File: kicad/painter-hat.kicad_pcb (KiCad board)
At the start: 2 copper layers, 64.6 x 55.8 mm, 45 parts, among them J1 Conn_01x08_Socket, J10 10137064-00021LF, J2 Conn_01x08_Socket, J3 Conn_01x08_Socket, J4 Conn_01x08_Socket, J5 Conn_02x20_Odd_Even, J6 Conn_01x04, J8 Conn_01x06_Pin, J9 Conn_01x04, Q1 NPN, Q2 NPN, Q4 Si2319CDS, Q5 Si2319CDS, U1 MAX26405AFOAY+T, U2 CYPD3177-24LQ, Y2 16 MHz

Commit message: feat: v2
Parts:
- removed J8: Conn_01x06_Pin, Connector_PinHeader_2.54mm:PinHeader_1x06_P2.54mm_Vertical
- removed Q1, Q2: NPN, Package_TO_SOT_THT:TO-92L_Inline_Wide
- removed Q5: Si2319CDS, Package_TO_SOT_SMD:SOT-23
- removed R1, R2, R3, R4: R, Resistor_SMD:R_0603_1608Metric
- added C12: 10uF, Capacitor_SMD:C_0603_1608Metric, F.Cu at (84.5, 94.1)
- added C13: 4.7uF, Capacitor_SMD:C_0603_1608Metric, F.Cu at (82.0, 92.6)
- added C14: 22uF, Capacitor_SMD:C_0805_2012Metric, F.Cu at (86.5, 86.1)
- added C15: 22uF, Capacitor_SMD:C_0805_2012Metric, F.Cu at (84.0, 86.1)
- added C16: 22uF, Capacitor_SMD:C_0805_2012Metric, F.Cu at (81.5, 86.1)
- added C17: 4.7uF, Capacitor_SMD:C_0603_1608Metric, F.Cu at (89.5, 93.8)
- added C18: 2.2uF, Capacitor_SMD:C_0603_1608Metric, F.Cu at (89.5, 91.3)
- added C19: 10nF, Capacitor_SMD:C_0402_1005Metric, F.Cu at (99.7, 98.0)
- added C20: 10nF, Capacitor_SMD:C_0402_1005Metric, F.Cu at (110.8, 89.6)
- added C21: 10nF, Capacitor_SMD:C_0402_1005Metric, F.Cu at (110.8, 90.8)
- added C22: 1uF, Capacitor_SMD:C_0805_2012Metric, F.Cu at (100.6, 130.0)
- added C23: 1uF, Capacitor_SMD:C_0805_2012Metric, F.Cu at (104.2, 129.5)
- added C24: 10uF, Capacitor_SMD:C_0805_2012Metric, F.Cu at (95.8, 129.8)
- added C25: 0.1uF, Resistor_SMD:R_0402_1005Metric, F.Cu at (82.6, 105.6)
- added C26: 2.2uF, Capacitor_SMD:C_0603_1608Metric, F.Cu at (84.6, 96.0)
- added D1: B340B-13-F, Diode_SMD:D_SMB, F.Cu at (97.4, 124.3)
- added G***: LOGO, Own:hackclub-logo, B.Cu at (81.7, 92.8)
- added G***: LOGO, Own:logo-vivid-v, B.Cu at (98.1, 110.0)
- added J7: Conn_01x06, Connector_PinSocket_2.54mm:PinSocket_1x06_P2.54mm_Vertical, F.Cu at (96.6, 85.3)
- added L2: 3.3-4.7uH, Inductor_SMD:L_Coilcraft_XxL4030, F.Cu at (90.0, 88.1)
- added Q3: FDS8949, Own:SOIC8_3P9X4P9_OSI, F.Cu at (102.6, 124.4)
- added R14: 10k, Resistor_SMD:R_0402_1005Metric, F.Cu at (111.2, 92.8)
- added R15: 10k, Capacitor_SMD:C_0603_1608Metric, F.Cu at (98.6, 129.8)
- added R16: 50k, Capacitor_SMD:C_0603_1608Metric, F.Cu at (92.8, 122.1)
- added R17: 1k, Capacitor_SMD:C_0603_1608Metric, F.Cu at (89.0, 115.4)
- added R18: 1k, Resistor_SMD:R_0402_1005Metric, F.Cu at (87.7, 115.3)
- added R19: 49.9k, Resistor_SMD:R_0402_1005Metric, F.Cu at (109.0, 131.1)
- added SW1: SW_Push, Button_Switch_SMD:SW_Push_1P1T_NO_CK_KMR2, F.Cu at (97.2, 103.0)
- added SW2: SW_Push, Button_Switch_SMD:SW_Push_1P1T_NO_CK_KMR2, F.Cu at (101.0, 103.0)
- added U3: MAX26405AFOAY+T, Own:FC2QFN-17, F.Cu at (85.3, 90.5)
- added U4: STM32F103CB, Package_QFP:LQFP-48_7x7mm_P0.5mm, F.Cu at (104.6, 92.1)
- C1: value 12uF -> 4.7uF; footprint Capacitor_SMD:C_0603_1608Metric -> Capacitor_SMD:C_0402_1005Metric
- C10, C11, C8: footprint Capacitor_SMD:C_0603_1608Metric -> Capacitor_SMD:C_0402_1005Metric
- C2, C3: value 4.7uF -> 100nF; footprint Capacitor_SMD:C_0603_1608Metric -> Capacitor_SMD:C_0402_1005Metric
- C4: value 2.2uF -> 100nF; footprint Capacitor_SMD:C_0603_1608Metric -> Capacitor_SMD:C_0402_1005Metric
- C5, C6: value 22uF -> 100nF; footprint Capacitor_SMD:C_0805_2012Metric -> Capacitor_SMD:C_0402_1005Metric
- C7: value 22uF -> 1uF; footprint Capacitor_SMD:C_0805_2012Metric -> Capacitor_SMD:C_0603_1608Metric
- C9: footprint Resistor_SMD:R_0603_1608Metric -> Capacitor_SMD:C_0402_1005Metric
- J1, J2, J3, J4: footprint Connector_PinHeader_2.54mm:PinHeader_1x08_P2.54mm_Vertical -> Connector_PinSocket_2.54mm:PinSocket_1x08_P2.54mm_Vertical
- J10: value 10137064-00021LF -> UJ40-C-H-G-SMT-P24-TR; footprint Ampheon-10137064-00021LF:AMPHENOL_10137064-00021LF -> Own:SAMESKY_UJ40-C-H-G-SMT-P24-TR
- L1: value 3.3-4.7uH -> 4.7uH; footprint Inductor_SMD:L_Coilcraft_XxL4030 -> Own:IND_NRS5030T100MMGJ_TAY
- Q4: value Si2319CDS -> FDS8949; footprint Package_TO_SOT_SMD:SOT-23-3 -> Own:SOIC8_3P9X4P9_OSI
- R10, R11, R12, R9: footprint Resistor_SMD:R_0603_1608Metric -> Resistor_SMD:R_0402_1005Metric
- R13: value 2.2k -> 10k; footprint Resistor_SMD:R_0603_1608Metric -> Resistor_SMD:R_0402_1005Metric
- R5: value R -> bridge; footprint Resistor_SMD:R_0603_1608Metric -> Resistor_SMD:R_0402_1005Metric
- R6, R8: value R -> 5.1k; footprint Resistor_SMD:R_0603_1608Metric -> Resistor_SMD:R_0402_1005Metric
- R7: value R -> dont connect; footprint Resistor_SMD:R_0603_1608Metric -> Resistor_SMD:R_0402_1005Metric
- U1: value MAX26405AFOAY+T -> TS30013-M033QFNR; footprint Own:FC2QFN-17 -> Own:QFN16_3X3_SEM
- moved J6 63.7 mm to (138.2, 91.0), turned to -90 degrees
- moved J9 58.6 mm to (138.2, 115.0), turned to -90 degrees
- moved J1 58.1 mm to (132.4, 86.7), turned to 0 degrees
- moved J4 50.0 mm to (117.2, 127.0), turned to 180 degrees
- moved L1 48.7 mm to (88.9, 102.4), turned to 180 degrees
- moved U1 46.1 mm to (83.4, 103.1), turned to -90 degrees
- moved J3 45.6 mm to (132.5, 109.3), turned to 0 degrees
- moved C10 43.1 mm to (92.4, 118.2)
- moved C9 42.9 mm to (92.4, 119.2)
- moved C8 42.8 mm to (92.4, 120.2)
- moved C11 38.4 mm to (93.2, 117.2), turned to 180 degrees
- moved U2 38.3 mm to (88.7, 119.6)
- moved J10 37.6 mm to (89.0, 129.2)
- moved R13 37.3 mm to (80.9, 101.9), turned to 90 degrees
- moved R7 36.1 mm to (93.8, 115.6), turned to 90 degrees
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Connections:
- net Net-(J8-Pin_1) renamed /Power/~{HP INT}
- net Net-(J8-Pin_5) renamed I2C1_SDA
- net Net-(J8-Pin_6) renamed I2C1_SCL
- C1 pad 1: Net-(U1-BST) -> VDD
- C1 pad 2: Net-(U1-LX) -> GND
- C2 pad 1: Net-(C2-Pad1) -> VDD
- C3 pad 1: GND -> VDD
- C3 pad 2: Net-(C3-Pad2) -> GND
- C4 pad 1: Net-(U1-BIAS) -> VDD
- C5 pad 1: GND -> VDD
- C5 pad 2: +5V -> GND
- C6 pad 1: GND -> VDD
- C6 pad 2: +5V -> GND
- C7 pad 1: GND -> VDD
- C7 pad 2: +5V -> GND
- J10 pad A9: unconnected-(J10-VBUS_A__1-PadA9) -> VBUS
- J10 pad B9: unconnected-(J10-VBUS_B__1-PadB9) -> VBUS
- J2 pad 1: Net-(J2-Pin_1) -> /Enable 1
- J2 pad 2: /Config 1_1 -> /MS 1_1
- J2 pad 3: /Config 1_2 -> /MS 1_2
- J2 pad 4: /Config 1_3 -> /UART2_TX
- J2 pad 5: /Config 1_4 -> /UART2_RX
- J4 pad 1: Net-(J4-Pin_1) -> /Enable 2
- J4 pad 2: /Config 2_1 -> /MS 2_1
- J4 pad 3: /Config 2_2 -> /MS 2_2
- J4 pad 4: /Config 2_3 -> /UART3_TX
- J4 pad 5: /Config 2_4 -> /UART3_RX
- J5 pad 11: /Config 1_2 -> unconnected-(J5-Pin_11-Pad11)
- J5 pad 12: /Step 2 -> unconnected-(J5-Pin_12-Pad12)
- J5 pad 13: /Config 2_3 -> unconnected-(J5-Pin_13-Pad13)
- J5 pad 14: GND -> unconnected-(J5-Pin_14-Pad14)
- J5 pad 15: /Config 2_2 -> unconnected-(J5-Pin_15-Pad15)
- J5 pad 18: /Direction 2 -> unconnected-(J5-Pin_18-Pad18)
- J5 pad 19: unconnected-(J5-Pin_19-Pad19) -> /SPI1_MOSI
- J5 pad 20: GND -> unconnected-(J5-Pin_20-Pad20)
- J5 pad 21: unconnected-(J5-Pin_21-Pad21) -> /SPI1_MISO
- J5 pad 23: unconnected-(J5-Pin_23-Pad23) -> /SPI1_SCK
- J5 pad 25: GND -> unconnected-(J5-Pin_25-Pad25)
- J5 pad 30: GND -> unconnected-(J5-Pin_30-Pad30)
- J5 pad 31: /Config 2_4 -> unconnected-(J5-Pin_31-Pad31)
- J5 pad 32: /Enable 1 -> unconnected-(J5-Pin_32-Pad32)
- J5 pad 33: /Direction 1 -> unconnected-(J5-Pin_33-Pad33)
- J5 pad 34: GND -> unconnected-(J5-Pin_34-Pad34)
- J5 pad 35: /Step 1 -> unconnected-(J5-Pin_35-Pad35)
- J5 pad 36: /Config 1_1 -> unconnected-(J5-Pin_36-Pad36)
- J5 pad 37: /Config 1_4 -> unconnected-(J5-Pin_37-Pad37)
- J5 pad 38: /Config 1_3 -> unconnected-(J5-Pin_38-Pad38)
- J5 pad 39: GND -> unconnected-(J5-Pin_39-Pad39)
- J5 pad 40: /Config 2_1 -> unconnected-(J5-Pin_40-Pad40)
- J5 pad 7: /Enable 2 -> unconnected-(J5-Pin_7-Pad7)
- L1 pad 1: +5V -> Net-(C25-Pad1)
- L1 pad 2: Net-(U1-LX) -> VDD
- Q4 pad 1: Net-(Q4-G) -> VBUS
- Q4 pad 2: VD -> Net-(Q4-Pad2)
- Q4 pad 3: VBUS -> +5V
- R10 pad 2: +3.3V -> GND
- R11 pad 2: +3.3V -> GND
- R12 pad 2: +3.3V -> GND
- R13 pad 1: Net-(J8-Pin_2) -> Net-(U1-PG)
- R13 pad 2: +3.3V -> VDD
- U1 pad 1: VD -> Net-(C25-Pad1)
- U1 pad 10: GND -> Net-(U1-BST)
- U1 pad 11: Net-(U1-BIAS) -> VD
- U1 pad 12: Net-(U1-BIAS) -> Net-(C25-Pad1)
- U1 pad 13: +5V -> Net-(C25-Pad1)
- U1 pad 14: unconnected-(U1-VEA-Pad14) -> GND
- U1 pad 15: unconnected-(U1-PGOOD-Pad15) -> GND
- U1 pad 16: Net-(U1-BIAS) -> Net-(C25-Pad1)
- U1 pad 17: unconnected-(U1-SYNCOUT-Pad17) -> GND
- U1 pad 2: Net-(U1-BST) -> VD
- U1 pad 3: Net-(C2-Pad1) -> VD
- U1 pad 5: GND -> VDD
- U1 pad 6: Net-(U1-LX) -> unconnected-(U1-NC-Pad6)
- U1 pad 7: GND -> unconnected-(U1-NC-Pad7)
- U1 pad 9: Net-(C3-Pad2) -> VD
- U2 pad 3: Net-(Q4-G) -> Net-(U2-VBUS_FET_EN)
- U2 pad 4: Net-(Q5-G) -> /Power/SAFE PWR
- U2 pad 8: Net-(J8-Pin_2) -> unconnected-(U2-GPIO_1-Pad8)
- U2 pad 9: Net-(J8-Pin_3) -> unconnected-(U2-FAULT-Pad9)
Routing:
- net GND: track 390.2 -> 106.7 mm, vias 3 -> 50
- net VDD: track 0.00 -> 95.9 mm, vias 0 -> 7
- net /Config 1_2: track 92.0 -> 0.00 mm, vias 3 -> 0
- net VD: track 79.0 -> 162.3 mm, vias 2 -> 6
- net /Config 1_1: track 74.9 -> 0.00 mm
- net /Config 1_3: track 59.7 -> 0.00 mm
- net /Config 2_1: track 57.3 -> 0.00 mm
- net /Config 1_4: track 52.2 -> 0.00 mm
- net /Enable 1: track 73.3 -> 22.0 mm, vias 3 -> 0
- net Net-(C22-Pad2): track 0.00 -> 45.2 mm
- net /NRST: track 0.00 -> 43.7 mm, vias 0 -> 2
- net /MS 2_1: track 0.00 -> 43.2 mm, vias 0 -> 2
- net Net-(Q4-Pad2): track 0.00 -> 41.3 mm, vias 0 -> 2
- net /MS 2_2: track 0.00 -> 40.8 mm, vias 0 -> 2
- net I2C1_SCL: track 15.9 -> 54.9 mm, vias 0 -> 6
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- added copper zone on B.Cu, net GND
- added copper zone on F.Cu, net GND
- removed copper zone on F.Cu, net VD
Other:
- outline, holes or cut-outs redrawn
- board text added: "DIR"
- board text added: "painter-hat v2 made by vividsystem"

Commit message: feat: v2.1
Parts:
- removed J10: UJ40-C-H-G-SMT-P24-TR, Own:SAMESKY_UJ40-C-H-G-SMT-P24-TR
- removed L2: 3.3-4.7uH, Inductor_SMD:L_Coilcraft_XxL4030
- removed U3: MAX26405AFOAY+T, Own:FC2QFN-17
- added C27: 100uF, Capacitor_SMD:C_Elec_8x10.2, F.Cu at (123.6, 125.9)
- added C28: 100uF, Capacitor_SMD:C_Elec_8x10.2, F.Cu at (123.6, 113.7)
- added C29: 0.47uF, Capacitor_SMD:C_0402_1005Metric, F.Cu at (85.1, 96.2)
- added C30: 100uF, Capacitor_SMD:C_Elec_8x10.2, F.Cu at (123.6, 101.5)
- added C31: 100uF, Capacitor_SMD:C_Elec_8x10.2, F.Cu at (123.6, 89.3)
- added C32: 1uF, Capacitor_SMD:C_0402_1005Metric, F.Cu at (80.8, 88.0)
- added C33: 2.2uF, Capacitor_SMD:C_0402_1005Metric, F.Cu at (85.1, 95.2)
- added L3: 5.2uH, easyeda2kicad:IND-SMD_4P-L10.5-W9.5-TL, F.Cu at (90.5, 107.3)
- added R1: 100k, Resistor_SMD:R_0603_1608Metric, F.Cu at (81.5, 90.1)
- added R2: 10k, Resistor_SMD:R_0402_1005Metric, F.Cu at (78.7, 90.7)
- added R20: 24.9k, Resistor_SMD:R_0603_1608Metric, F.Cu at (79.9, 90.1)
- added R3: 75k, Resistor_SMD:R_0603_1608Metric, F.Cu at (85.3, 92.0)
- added R4: 4.07k, Resistor_SMD:R_0603_1608Metric, F.Cu at (85.3, 90.4)
- added U5: LM76005RNPR, easyeda2kicad:WQFN-30_L6.0-W4.0-P0.50-TL-EP_LM76005RNPR, F.Cu at (81.4, 95.3)
- added USBC1: TYPE-C-31-M-12, easyeda2kicad:USB-C_SMD-TYPE-C-31-M-12, F.Cu at (89.0, 126.7)
- C1: footprint Capacitor_SMD:C_0402_1005Metric -> Capacitor_SMD:C_0603_1608Metric
- C12: footprint Capacitor_SMD:C_0603_1608Metric -> Capacitor_SMD:C_0805_2012Metric
- C13: value 4.7uF -> 10uF; footprint Capacitor_SMD:C_0603_1608Metric -> Capacitor_SMD:C_0805_2012Metric
- C14: value 22uF -> 100uF; footprint Capacitor_SMD:C_0805_2012Metric -> Capacitor_SMD:C_Elec_8x10.2
- C15, C16: value 22uF -> 47uF
- C17: value 4.7uF -> 47uF; footprint Capacitor_SMD:C_0603_1608Metric -> Capacitor_SMD:C_0805_2012Metric
- C18: value 2.2uF -> 10nF; footprint Capacitor_SMD:C_0603_1608Metric -> Capacitor_SMD:C_0402_1005Metric
- C26: value 2.2uF -> 100pF; footprint Capacitor_SMD:C_0603_1608Metric -> Capacitor_SMD:C_0402_1005Metric
- C7: footprint Capacitor_SMD:C_0603_1608Metric -> Capacitor_SMD:C_0402_1005Metric
- R16: footprint Capacitor_SMD:C_0603_1608Metric -> Resistor_SMD:R_0603_1608Metric
- moved C25 22.9 mm to (89.8, 83.9), turned to 0 degrees
- moved R13 21.5 mm to (92.7, 83.9), turned to 0 degrees
- moved C14 20.3 mm to (81.0, 105.6), turned to 90 degrees
- moved C13 19.4 mm to (83.8, 111.9)
- moved C12 19.1 mm to (78.2, 112.1), turned to -90 degrees
- moved U1 18.5 mm to (91.5, 86.5), turned to 180 degrees
- moved Y1 17.7 mm to (111.1, 103.9), turned to 0 degrees
- moved C15 14.9 mm to (91.5, 99.0)
- moved C16 14.7 mm to (88.5, 99.0)
- moved L1 10.8 mm to (91.7, 92.0), turned to 0 degrees
- moved J6 8.42 mm to (137.2, 99.3), turned to 90 degrees
- moved C26 7.56 mm to (82.9, 88.7), turned to -90 degrees
- moved J9 6.76 mm to (136.9, 121.6), turned to 90 degrees
- moved C17 6.40 mm to (85.7, 99.0), turned to -90 degrees
- moved C18 6.23 mm to (83.3, 90.9), turned to 90 degrees
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- renumbered SW2 to BOOT, SW1 to RST, Y2 to Y1
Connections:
- C12 pad 1: Net-(U3-BST) -> VD
- C12 pad 2: Net-(U3-LX) -> GND
- C13 pad 1: Net-(C13-Pad1) -> VD
- C14 pad 1: GND -> VD
- C14 pad 2: +5V -> GND
- C15 pad 1: GND -> +5V
- C15 pad 2: +5V -> GND
- C16 pad 1: GND -> +5V
- C16 pad 2: +5V -> GND
- C17 pad 1: GND -> +5V
- C17 pad 2: Net-(C17-Pad2) -> GND
- C26 pad 1: Net-(U3-BST) -> +5V
- C26 pad 2: Net-(U3-LX) -> Net-(U5-FB)
- U4 pad 18: /Direction 2 -> /Step 1
- U4 pad 19: /Step 2 -> /Direction 1
- U4 pad 3: unconnected-(U4-PC14-Pad3) -> /CLK 1
- U4 pad 39: /Enable 1 -> /Step 2
- U4 pad 40: /MS 1_1 -> /Direction 2
- U4 pad 41: /MS 1_2 -> /Enable 1
- U4 pad 45: /Step 1 -> /MS 1_1
- U4 pad 46: /Direction 1 -> /MS 1_2
- Y1 pad 1: +5V -> VDD
- Y1 pad 4: +5V -> VDD
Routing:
- net VD: track 162.3 -> 46.2 mm, vias 6 -> 14
- net VDD: track 95.9 -> 44.4 mm, vias 7 -> 5
- net Net-(U3-LX): track 17.2 -> 0.00 mm
- net Net-(C29-Pad2): track 0.00 -> 16.0 mm
- net /Motor1_A: track 20.5 -> 7.33 mm
- net /UART2_RX: track 26.5 -> 14.4 mm, vias 0 -> 1
- net /Motor3_A: track 19.2 -> 7.12 mm
- net I2C1_SCL: track 54.9 -> 43.0 mm, vias 6 -> 4
- net /UART2_TX: track 26.5 -> 14.7 mm, vias 0 -> 1
- net Net-(U3-BST): track 11.4 -> 0.00 mm
- net Net-(C22-Pad2): track 45.2 -> 34.4 mm, vias 0 -> 2
- net /NRST: track 43.7 -> 33.4 mm, vias 2 -> 1
- net /Step 1: track 25.5 -> 16.8 mm, vias 0 -> 1
- net /Direction 1: track 26.0 -> 19.3 mm, vias 0 -> 1
- net /Direction 2: track 28.7 -> 23.0 mm, vias 2 -> 1
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- added copper zone on In2.Cu, net +5V
- added copper zone on In1.Cu, net GND
- added copper zone on In2.Cu, net VD
- added copper zone on In2.Cu, net VDD
- removed copper zone on F.Cu, net GND
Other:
- copper layers 2 -> 4

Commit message: feat: updated everything
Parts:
- added C27: 100uF, Capacitor_SMD:C_Elec_8x10.2, F.Cu at (152.1, 93.7)
- added C28: 100uF, Capacitor_SMD:C_Elec_8x10.2, F.Cu at (152.0, 105.2)
- added C30: 100uF, Capacitor_SMD:C_Elec_8x10.2, F.Cu at (152.0, 128.9)
- added C31: 100uF, Capacitor_SMD:C_Elec_8x10.2, F.Cu at (152.0, 117.1)
- C25: value 0.1uF -> 100nF
- R7: value dont connect -> leave open
- turned C14 to -90 degrees
- renumbered RST to SW1, BOOT to SW2
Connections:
- USBC1 pad 1: GND -> (no net)
- USBC1 pad 2: GND -> (no net)
- USBC1 pad 3: GND -> (no net)
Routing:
- net +5V: track 171.9 -> 173.3 mm

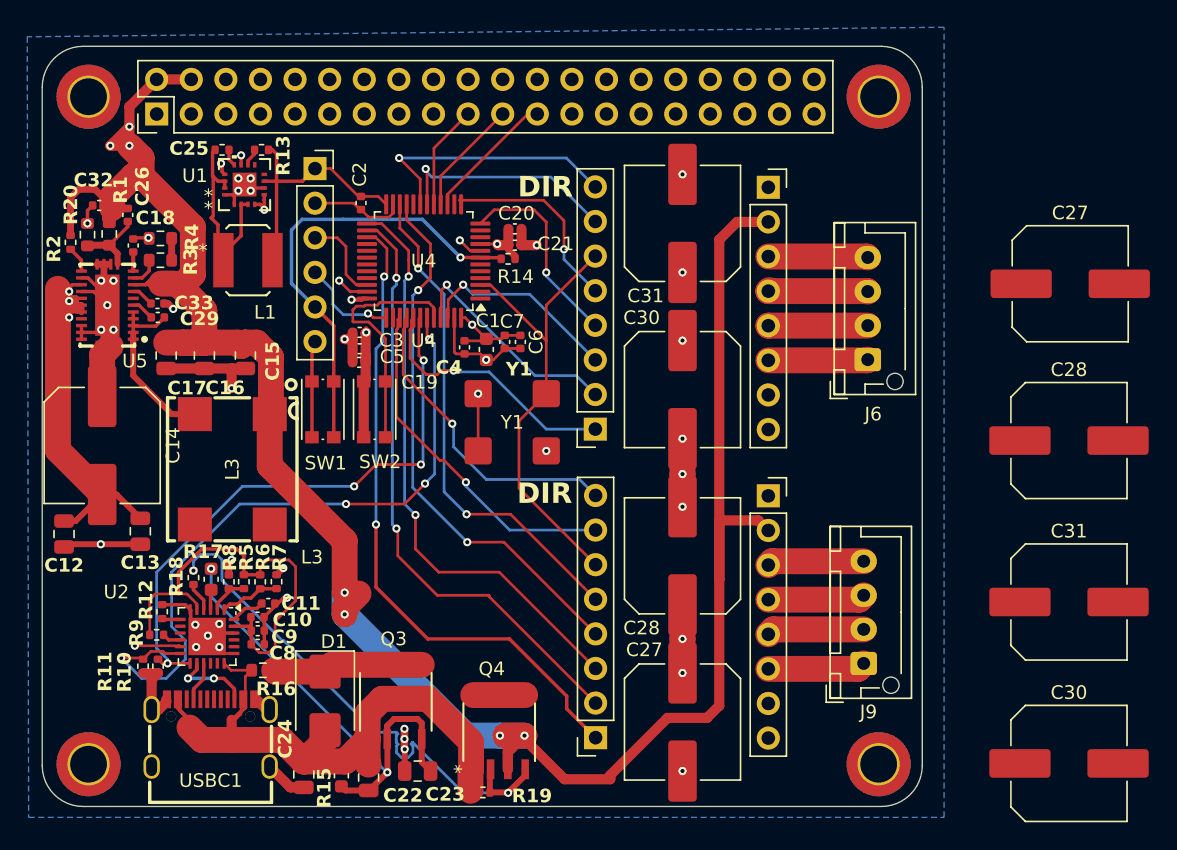
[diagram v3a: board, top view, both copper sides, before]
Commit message: feat(v2.1.1): BOOT0, NRST Wiring, Polarized Caps fixed
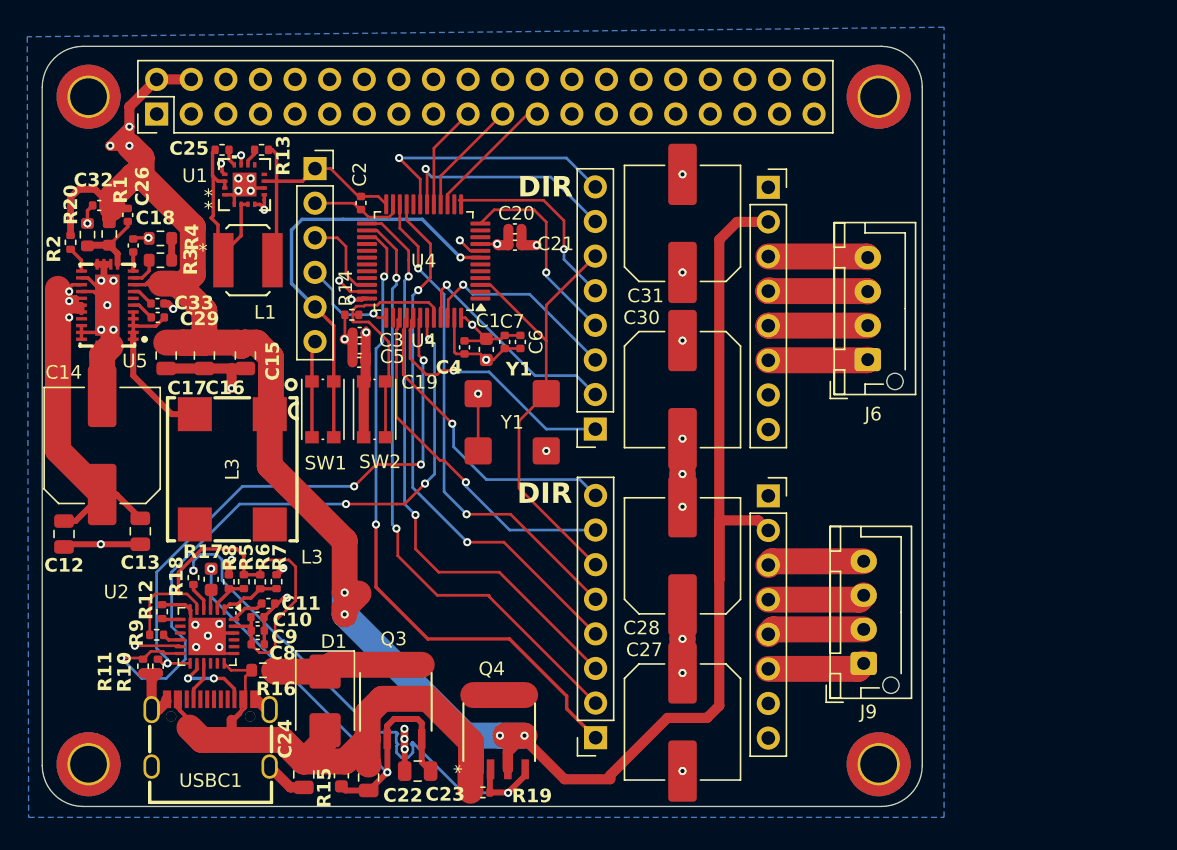
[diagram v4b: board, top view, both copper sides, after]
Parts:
- removed the C27 at (152.1, 93.7)
- removed the C28 at (152.0, 105.2)
- removed the C30 at (152.0, 128.9)
- removed the C31 at (152.0, 117.1)
- moved R14 12.2 mm to (99.3, 96.0), turned to 0 degrees
- turned C14 to 90 degrees
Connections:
- R14 pad 1: VDD -> GND
- R14 pad 2: /NRST -> Net-(U4-BOOT0)
- USBC1 pad 1: (no net) -> GND
- USBC1 pad 2: (no net) -> GND
- USBC1 pad 3: (no net) -> GND
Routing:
- net GND: track 104.1 -> 105.9 mm
- net /NRST: track 33.4 -> 31.9 mm
- net VDD: track 44.4 -> 43.2 mm
- net Net-(U4-BOOT0): track 18.1 -> 18.7 mm

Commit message: feat: added community designs
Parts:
- added G***: LOGO, Own:pepe-meme, B.Cu at (96.5, 110.7)
- added G***: LOGO, Own:breaker, B.Cu at (122.9, 97.0)
- moved G*** 29.0 mm to (123.3, 124.4)
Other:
- board text removed: "painter-hat v2 made by vividsystem"
